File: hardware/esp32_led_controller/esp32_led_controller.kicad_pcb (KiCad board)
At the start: 4 copper layers, 114 x 153 mm, 556 parts, among them J1 USB_B, J2 CONN_01X09, J3 CONN_01X08, J4 BARREL_JACK, J5 CONN_01X03, J6 USB_C_Receptacle_USB2.0, Q1 Q_NPN_BEC, Q2 Q_NPN_BEC, SW1 SW_Push, U1 MCP1415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

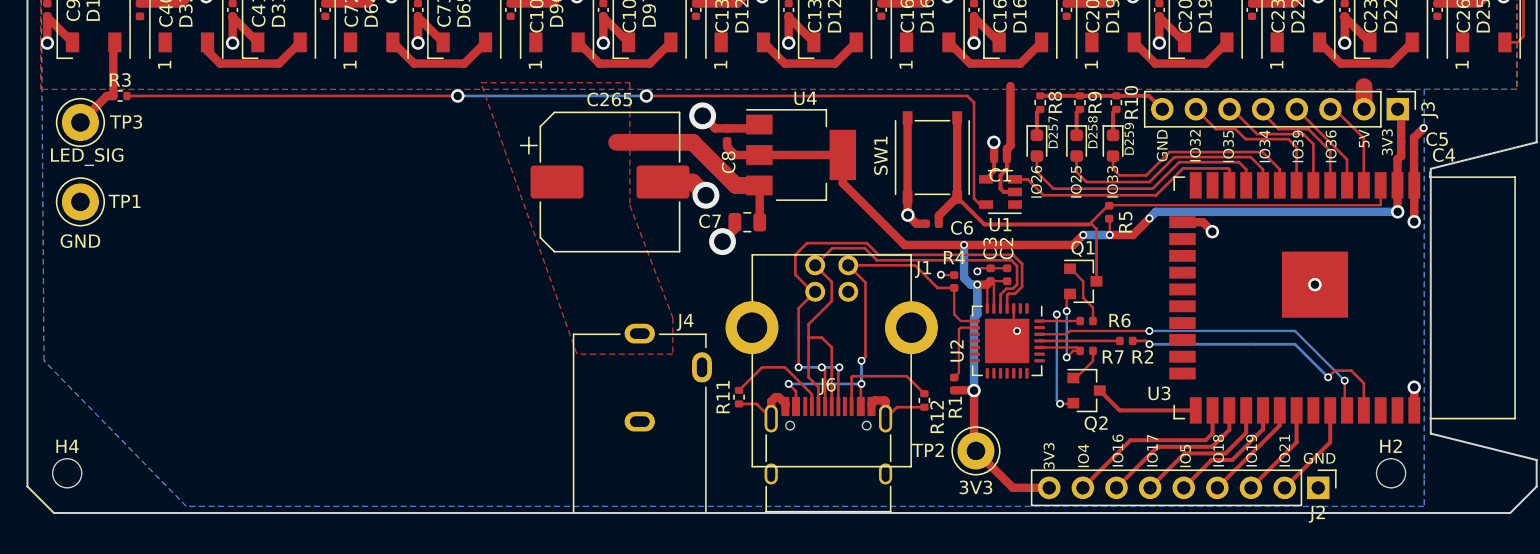
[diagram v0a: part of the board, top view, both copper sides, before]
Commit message: Improved silkscreen and added test points
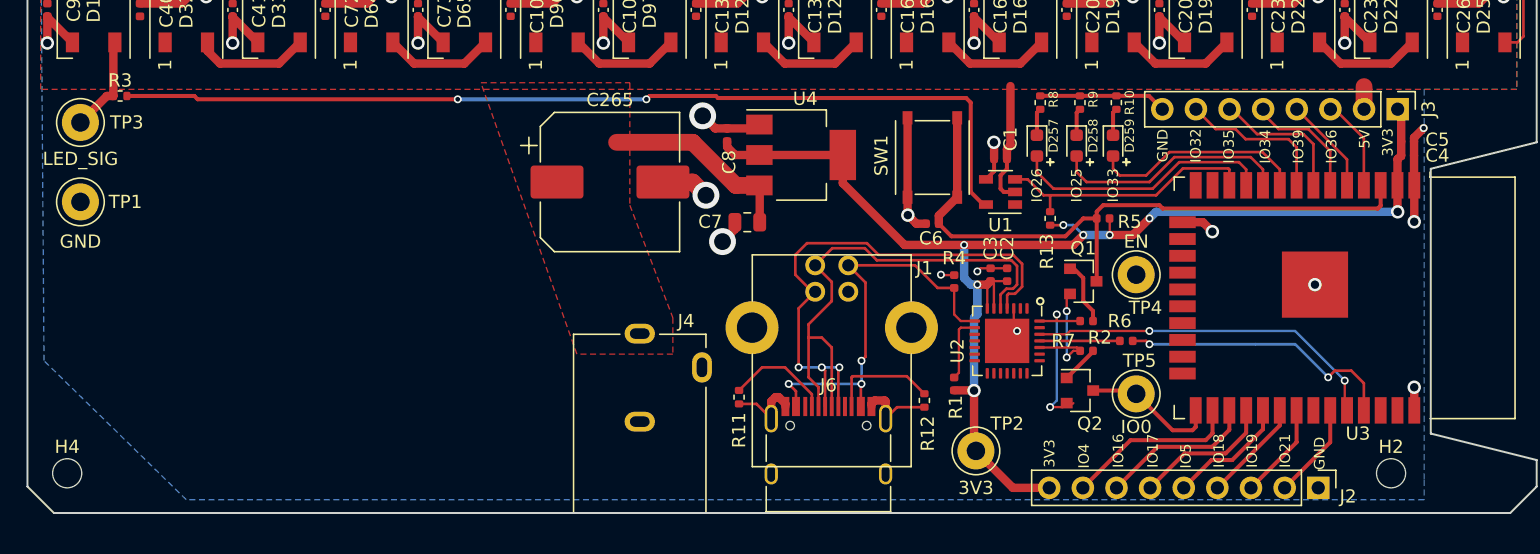
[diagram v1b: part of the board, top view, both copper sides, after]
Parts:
- added R13: 10kR, Resistor_SMD:R_0402_1005Metric, F.Cu at (205.2, 176.8)
- added TP4: TestPoint, TestPoint:TestPoint_Loop_D3.50mm_Drill1.4mm_Beaded, F.Cu at (211.8, 181.0)
- added TP5: TestPoint, TestPoint:TestPoint_Loop_D3.50mm_Drill1.4mm_Beaded, F.Cu at (211.8, 190.0)
- moved R5 0.66 mm to (209.2, 176.8), turned to 0 degrees
- moved Q2 0.50 mm to (207.5, 189.8)
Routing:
- net +3V3: track 97.0 -> 99.8 mm, vias 7 -> 8
- net /IO0: track 7.87 -> 10.3 mm
- net /EN: track 48.1 -> 50.2 mm
- net /DOUT: track 18.8 -> 20.0 mm
- net /USB_DTR: track 11.4 -> 12.2 mm
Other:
- board text added: "EN"
- board text added: "IO0"

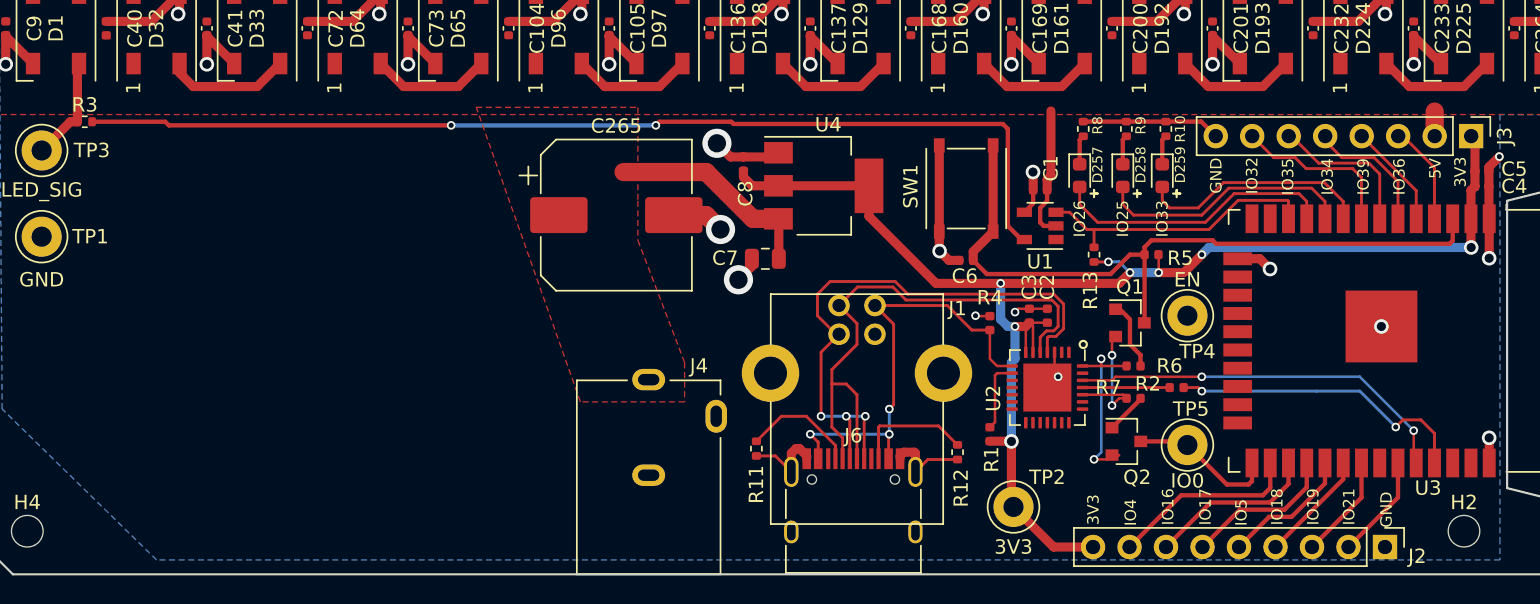
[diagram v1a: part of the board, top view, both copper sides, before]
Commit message: Added configuration jumpers
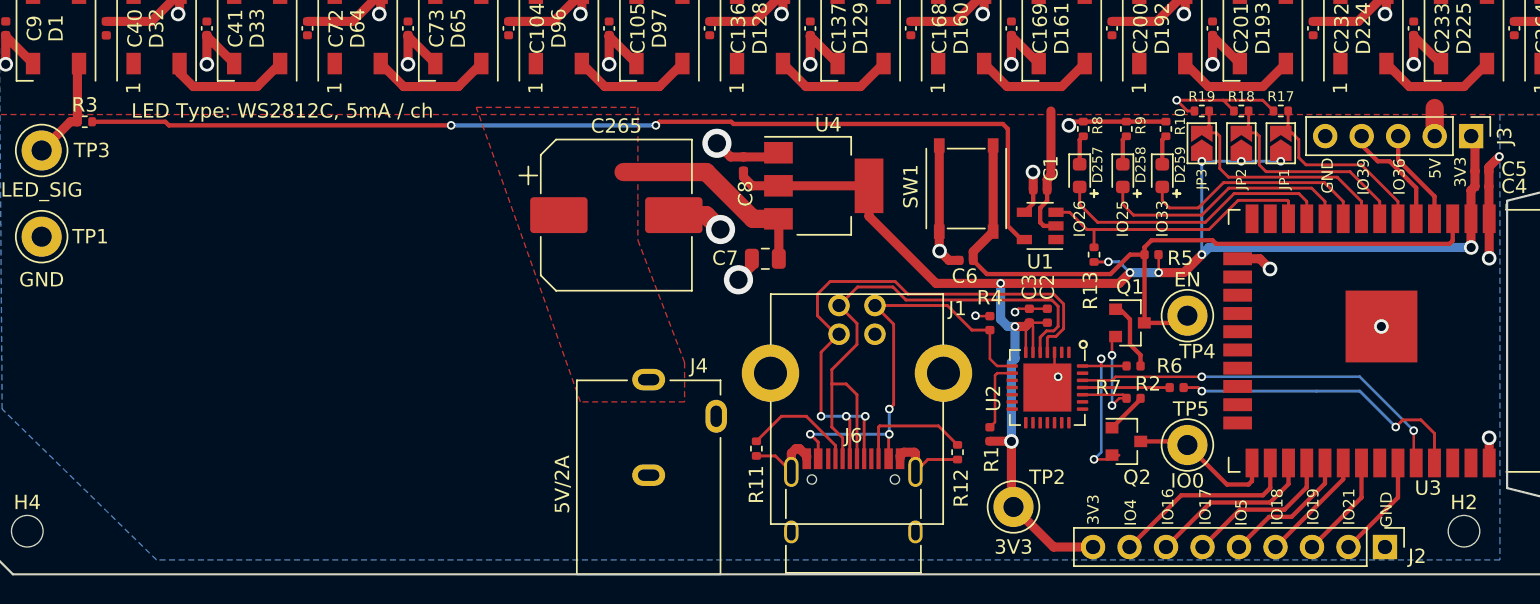
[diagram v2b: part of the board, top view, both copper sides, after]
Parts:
- added JP1: J_NO, Jumper:SolderJumper-2_P1.3mm_Open_TrianglePad1.0x1.5mm, F.Cu at (218.2, 169.0)
- added JP2: J_NO, Jumper:SolderJumper-2_P1.3mm_Open_TrianglePad1.0x1.5mm, F.Cu at (215.5, 169.0)
- added JP3: J_NO, Jumper:SolderJumper-2_P1.3mm_Open_TrianglePad1.0x1.5mm, F.Cu at (212.8, 169.0)
- added R17: 10kR, Resistor_SMD:R_0402_1005Metric, F.Cu at (218.2, 166.8)
- added R18: 10kR, Resistor_SMD:R_0402_1005Metric, F.Cu at (215.5, 166.8)
- added R19: 10kR, Resistor_SMD:R_0402_1005Metric, F.Cu at (212.8, 166.8)
- J3: value CONN_01X08 -> CONN_01X05; footprint Connector_PinHeader_2.54mm:PinHeader_1x08_P2.54mm_Vertical -> Connector_PinHeader_2.54mm:PinHeader_1x05_P2.54mm_Vertical
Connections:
- J3 pad 5: /IO34 -> GND
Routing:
- net +3V3: track 99.8 -> 113.4 mm, vias 8 -> 11
- net GND: track 1618.8 -> 1625.6 mm, vias 269 -> 271
- net /IO32: track 11.7 -> 17.3 mm
- net /IO35: track 10.5 -> 15.7 mm
- net /IO34: track 9.17 -> 13.8 mm
- net /EN: track 50.2 -> 53.4 mm
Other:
- board text added: "5V/2A"
- board text added: "LED Type: WS2812C, 5mA / ch"
- board text removed: "IO32"
- board text removed: "IO34"
- board text removed: "IO35"
